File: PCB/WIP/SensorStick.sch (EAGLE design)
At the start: 84 parts, among them U1 TPD4F003DQDR, U10 LIS3MDLTR, U11 LIS3MDLTR, U2 BMI088, U3 BMI088, U4 BMI088, U5 STM32H743ZIT6, U9 LIS3MDLTR, Y1 ECS-TXO-3225MV-400-TR

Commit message: starting on board
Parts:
- removed AIRSPEED: 4525DO-DS5AI001DP, 4525DO-DS5AI001DP:4525DO-DS5AI001DP
- removed C3: 0.1uF, SparkFun-Capacitors:0.1UF-0402-6.3V-10%-X7R
- added R19, R20, R21, R22: RT0402FRE07220RL, ce-capstone:RT0402FRE07220RL
- R6, R7: value 4.7k -> RT0402FRE07220RL; device SparkFun-Resistors:4.7KOHM-0603-1/10W-1% -> ce-capstone:RT0402FRE07220RL
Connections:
- new net N$13: R6.2, U5G$3.PD7
- new net N$14: R7.2, U5G$3.PD6
- net 3V3: no longer R6.2, R7.1
- net 5V: no longer AIRSPEED.VCC, C3.2
- net CSB_ACCEL1: now also R19.2
- net CSB_ACCEL2: now also R21.2
- net CSB_ACCEL3: now also R6.1
- net CSB_GYRO1: now also R20.2
- net CSB_GYRO2: now also R7.1
- net CSB_GYRO3: now also U5G$3.PD10
- net EXTI3: no longer AIRSPEED.INT_(I2C)_/_SS_(SPI)
- net GND: now also Y1.GROUND; no longer AIRSPEED.GROUND, C3.1
- net I2C3_SCL: no longer AIRSPEED.SCL_(I2C)_/_SCLK_(SPI), R6.1
- net I2C3_SDA: no longer AIRSPEED.SDA_(I2C)_/_MISO_(SPI), R7.2
- net SPI1_MISO: no longer U4.SDO2
- net SPI2_MISO: no longer U3.SDO2
- net SPI3_MISO: no longer U2.SDO2
- net USART2_RX: now also U5G$1.PA3
- net USART2_TX: now also U5G$1.PA2
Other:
- moved on the sheet: R11, R6, R7, R8, R9, Y1

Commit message: snapshot
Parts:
- removed R22: RT0402FRE07220RL, ce-capstone:RT0402FRE07220RL
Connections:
- net SPI1_CS renamed JTDI
- new net JTRST: U5G$2.PB4(!JTRST!)
- new net TRACESWO: U5G$2.PB3(JTDO/TRACESWO)
- net NRST: now also U5G$1.!RST
- net SPI3_MISO: now also U5G$2.PC11; no longer U5G$2.PB4(!JTRST!)
- net SPI3_SCK: now also U5G$2.PC10; no longer U5G$2.PB3(JTDO/TRACESWO)
- net SWCLK: now also U5G$1.PA14(JTCK/SWCLK)
- net SWDIO: now also U5G$1.PA13(JTMS-SWDIO)
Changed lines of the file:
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@@
 <part name="R20" library="ce-capstone" deviceset="RT0402FRE07220RL" device=""/>
 <part name="R21" library="ce-capstone" deviceset="RT0402FRE07220RL" device=""/>
-<part name="R22" library="ce-capstone" deviceset="RT0402FRE07220RL" device=""/>
 </parts>
 <sheets>
@@
 <instance part="R20" gate="G$1" x="147.32" y="147.32" smashed="yes"/>
 <instance part="R21" gate="G$1" x="147.32" y="144.78" smashed="yes"/>
-<instance part="R22" gate="G$1" x="200.66" y="134.62" smashed="yes">
-<attribute name="NAME" x="196.85" y="136.1186" size="1.778" layer="95"/>
-<attribute name="VALUE" x="196.85" y="131.318" size="1.778" layer="96"/>
-</instance>
 </instances>
 <busses>
@@
 <label x="215.9" y="172.72" size="1.778" layer="95"/>
 </segment>
+<segment>
+<pinref part="U5" gate="G$1" pin="!RST"/>
+<wire x1="106.68" y1="226.06" x2="116.84" y2="226.06" width="0.1524" layer="91"/>
+<label x="111.76" y="226.06" size="1.778" layer="95"/>
+</segment>
 </net>
 <net name="DP" class="0">
@@
 </segment>
 </net>
-<net name="SPI1_CS" class="0">
-<segment>
-<pinref part="U5" gate="G$1" pin="PA15(JTDI)"/>
-<wire x1="66.04" y1="187.96" x2="58.42" y2="187.96" width="0.1524" layer="91"/>
-<label x="55.88" y="187.96" size="1.778" layer="95"/>
-</segment>
-</net>
 <net name="I2C2_SDA" class="0">
 <segment>
@@
 <net name="SPI4_CS" class="0">
 <segment>
-<wire x1="144.78" y1="157.48" x2="154.94" y2="157.48" width="0.1524" layer="91"/>
-<label x="147.32" y="157.48" size="1.778" layer="95"/>
-<pinref part="U5" gate="G$3" pin="PE4"/>
-</segment>
-<segment>
 <pinref part="U9" gate="G$1" pin="CS"/>
 <wire x1="251.46" y1="33.02" x2="243.84" y2="33.02" width="0.1524" layer="91"/>
 <label x="241.3" y="33.02" size="1.778" layer="95"/>
 </segment>
+<segment>
+<pinref part="U5" gate="G$3" pin="PE4"/>
+<wire x1="144.78" y1="157.48" x2="154.94" y2="157.48" width="0.1524" layer="91"/>
+<label x="147.32" y="157.48" size="1.778" layer="95"/>
+</segment>
 </net>
 <net name="SPI5_CS" class="0">
-<segment>
-<wire x1="160.02" y1="180.34" x2="152.4" y2="180.34" width="0.1524" layer="91"/>
-<label x="149.86" y="180.34" size="1.778" layer="95"/>
-<pinref part="U5" gate="G$4" pin="PF6"/>
-</segment>
 <segment>
 <pinref part="U11" gate="G$1" pin="CS"/>
@@
 <label x="187.96" y="284.48" size="1.778" layer="95"/>
 </segment>
+<segment>
+<pinref part="U5" gate="G$4" pin="PF6"/>
+<wire x1="160.02" y1="180.34" x2="152.4" y2="180.34" width="0.1524" layer="91"/>
+<label x="149.86" y="180.34" size="1.778" layer="95"/>
+</segment>
 </net>
 <net name="SPI5_SCK" class="0">
@@
 <net name="SPI6_CS" class="0">
 <segment>
-<wire x1="195.58" y1="175.26" x2="205.74" y2="175.26" width="0.1524" layer="91"/>
-<label x="198.12" y="175.26" size="1.778" layer="95"/>
-<pinref part="U5" gate="G$4" pin="PG8"/>
-</segment>
-<segment>
 <pinref part="U10" gate="G$1" pin="CS"/>
 <wire x1="15.24" y1="287.02" x2="7.62" y2="287.02" width="0.1524" layer="91"/>
 <label x="5.08" y="287.02" size="1.778" layer="95"/>
 </segment>
+<segment>
+<pinref part="U5" gate="G$4" pin="PG8"/>
+<wire x1="195.58" y1="175.26" x2="203.2" y2="175.26" width="0.1524" layer="91"/>
+<wire x1="205.74" y1="175.26" x2="203.2" y2="175.26" width="0.1524" layer="91"/>
+<label x="198.12" y="175.26" size="1.778" layer="95"/>
+</segment>
 </net>
 <net name="I2C4_SCL" class="0">
@@
 <net name="SPI3_MISO" class="0">
 <segment>
-<wire x1="139.7" y1="243.84" x2="132.08" y2="243.84" width="0.1524" layer="91"/>
-<label x="127" y="243.84" size="1.778" layer="95"/>
-<pinref part="U5" gate="G$2" pin="PB4(!JTRST!)"/>
-</segment>
-<segment>
 <pinref part="U2" gate="G$1" pin="SDO1"/>
 <wire x1="327.66" y1="76.2" x2="335.28" y2="76.2" width="0.1524" layer="91"/>
 <label x="325.12" y="76.2" size="1.778" layer="95"/>
 </segment>
+<segment>
+<pinref part="U5" gate="G$2" pin="PC11"/>
+<wire x1="185.42" y1="226.06" x2="193.04" y2="226.06" width="0.1524" layer="91"/>
+<label x="187.96" y="226.06" size="1.778" layer="95"/>
+</segment>
 </net>
 <net name="SPI3_MOSI" class="0">
@@
 <net name="SPI3_SCK" class="0">
 <segment>
-<wire x1="139.7" y1="246.38" x2="132.08" y2="246.38" width="0.1524" layer="91"/>
-<label x="127" y="246.38" size="1.778" layer="95"/>
-<pinref part="U5" gate="G$2" pin="PB3(JTDO/TRACESWO)"/>
-</segment>
-<segment>
 <pinref part="U2" gate="G$1" pin="SCL/SCK"/>
 <wire x1="292.1" y1="66.04" x2="284.48" y2="66.04" width="0.1524" layer="91"/>
 <label x="281.94" y="66.04" size="1.778" layer="95"/>
 </segment>
+<segment>
+<pinref part="U5" gate="G$2" pin="PC10"/>
+<wire x1="185.42" y1="228.6" x2="193.04" y2="228.6" width="0.1524" layer="91"/>
+<label x="187.96" y="228.6" size="1.778" layer="95"/>
+</segment>
 </net>
 <net name="SPI2_SCK" class="0">
@@
 <pinref part="U1" gate="A" pin="CH3_IN"/>
 </segment>
+<segment>
+<pinref part="U5" gate="G$1" pin="PA13(JTMS-SWDIO)"/>
+<wire x1="66.04" y1="193.04" x2="55.88" y2="193.04" width="0.1524" layer="91"/>
+<label x="55.88" y="193.04" size="1.778" layer="95"/>
+</segment>
 </net>
 <net name="SWCLK" class="0">
@@
 <wire x1="276.86" y1="139.7" x2="256.54" y2="139.7" width="0.1524" layer="91"/>
 <pinref part="U1" gate="A" pin="CH2_IN"/>
+</segment>
+<segment>
+<pinref part="U5" gate="G$1" pin="PA14(JTCK/SWCLK)"/>
+<wire x1="66.04" y1="190.5" x2="55.88" y2="190.5" width="0.1524" layer="91"/>
+<label x="55.88" y="190.5" size="1.778" layer="95"/>
 </segment>
 </net>
@@
 </segment>
 </net>
+<net name="JTDI" class="0">
+<segment>
+<pinref part="U5" gate="G$1" pin="PA15(JTDI)"/>
+<wire x1="66.04" y1="187.96" x2="55.88" y2="187.96" width="0.1524" layer="91"/>
+<label x="55.88" y="187.96" size="1.778" layer="95"/>
+</segment>
+</net>
+<net name="TRACESWO" class="0">
+<segment>
+<pinref part="U5" gate="G$2" pin="PB3(JTDO/TRACESWO)"/>
+<wire x1="139.7" y1="246.38" x2="132.08" y2="246.38" width="0.1524" layer="91"/>
+<label x="129.54" y="246.38" size="1.778" layer="95"/>
+</segment>
+</net>
+<net name="JTRST" class="0">
+<segment>
+<pinref part="U5" gate="G$2" pin="PB4(!JTRST!)"/>
+<wire x1="139.7" y1="243.84" x2="132.08" y2="243.84" width="0.1524" layer="91"/>
+<label x="129.54" y="243.84" size="1.778" layer="95"/>
+</segment>
+</net>

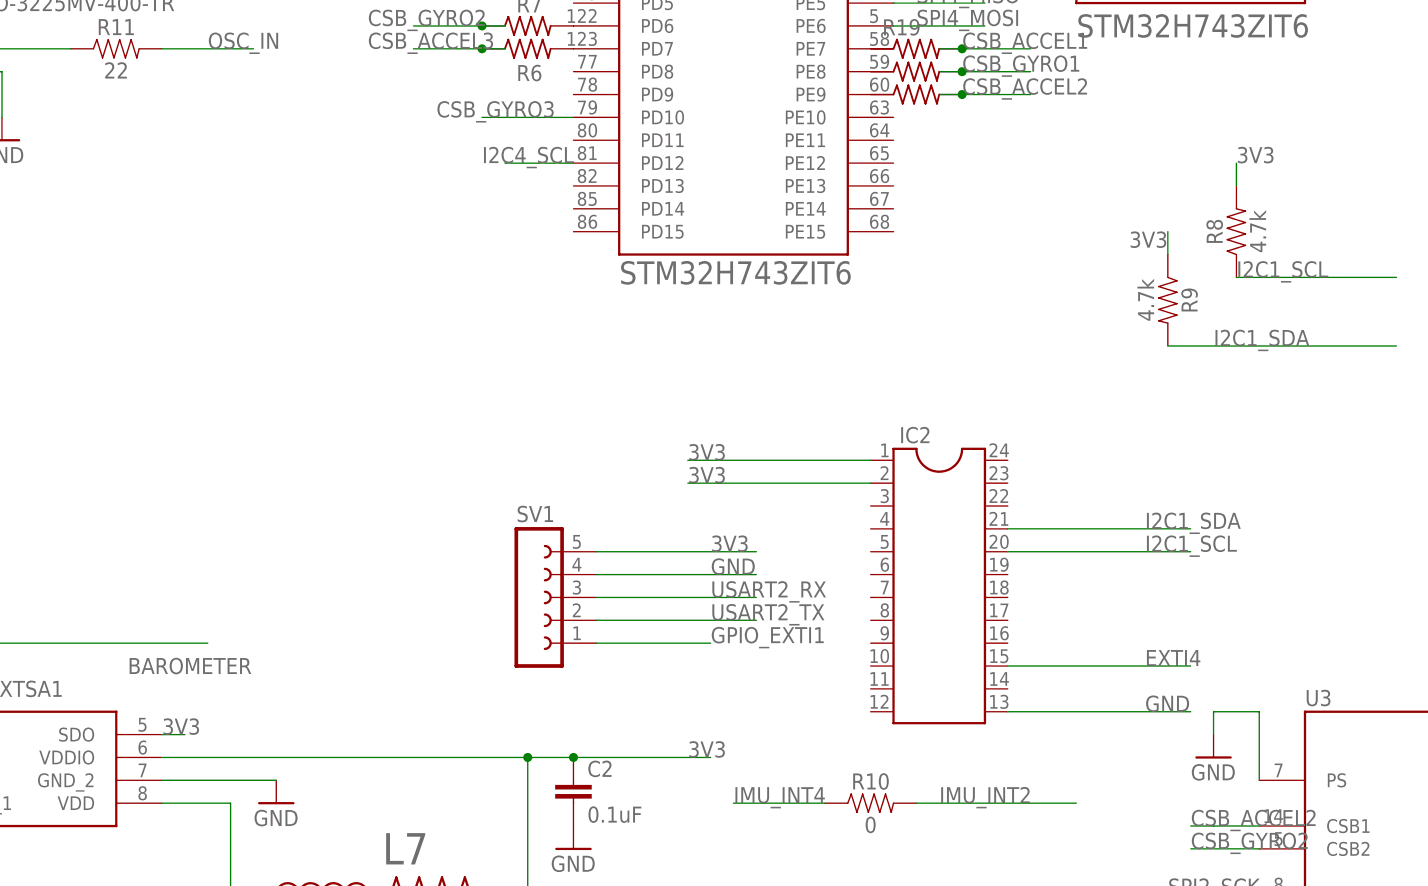
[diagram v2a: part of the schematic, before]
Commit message: added in JST connections, still need to resolve extra SPI connection
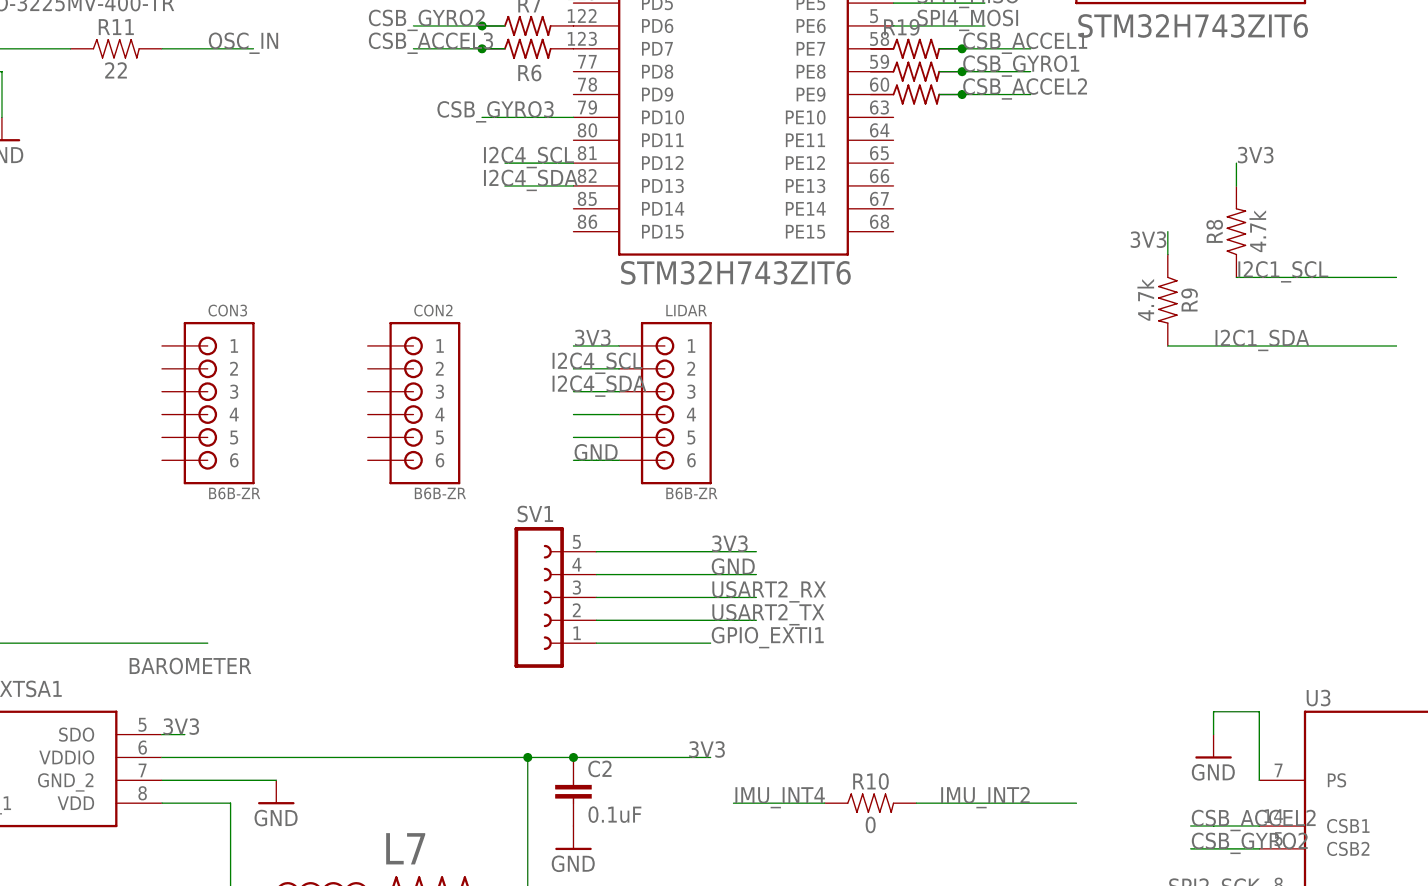
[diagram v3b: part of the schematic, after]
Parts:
- removed IC2: (no value), ic-package:DIL24-6
- added CON2, CON3, LIDAR: B6B-ZR, jst:B6B-ZR
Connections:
- new net N$21: LIDAR.5
- new net N$22: LIDAR.4
- net 3V3: now also LIDAR.1; no longer IC2.1, IC2.2
- net EXTI4: no longer IC2.15
- net GND: now also LIDAR.6; no longer IC2.13
- net I2C1_SCL: no longer IC2.20
- net I2C1_SDA: no longer IC2.21
- net I2C4_SCL: now also LIDAR.2
- net I2C4_SDA: now also LIDAR.3, U5G$3.PD13
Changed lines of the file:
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@@
 <part name="C27" library="capacitor-wima" library_urn="urn:adsk.eagle:library:116" deviceset="C" device="2.5/4" package3d_urn="urn:adsk.eagle:package:5408/1"/>
 <part name="JP7" library="pinhead" library_urn="urn:adsk.eagle:library:325" deviceset="PINHD-2X3" device="" package3d_urn="urn:adsk.eagle:package:22462/2"/>
-<part name="IC2" library="ic-package" library_urn="urn:adsk.eagle:library:239" deviceset="DIL24" device="-6" package3d_urn="urn:adsk.eagle:package:1009/2"/>
 <part name="U2" library="BMI088" deviceset="BMI088" device=""/>
 <part name="GND33" library="supply1" library_urn="urn:adsk.eagle:library:371" deviceset="GND" device=""/>
@@
 <part name="R20" library="ce-capstone" deviceset="RT0402FRE07220RL" device=""/>
 <part name="R21" library="ce-capstone" deviceset="RT0402FRE07220RL" device=""/>
+<part name="LIDAR" library="jst" deviceset="B6B-ZR" device=""/>
+<part name="CON2" library="jst" deviceset="B6B-ZR" device=""/>
+<part name="CON3" library="jst" deviceset="B6B-ZR" device=""/>
 </parts>
 <sheets>
@@
 <attribute name="VALUE" x="344.17" y="104.14" size="1.778" layer="96"/>
 </instance>
-<instance part="IC2" gate="G$1" x="149.86" y="88.9" smashed="yes">
-<attribute name="NAME" x="145.415" y="106.045" size="1.778" layer="95"/>
-<attribute name="VALUE" x="145.415" y="72.39" size="1.778" layer="96"/>
-</instance>
 <instance part="U2" gate="G$1" x="309.88" y="68.58" smashed="yes">
 <attribute name="NAME" x="297.18" y="86.995" size="1.778" layer="95"/>
@@
 <instance part="R20" gate="G$1" x="147.32" y="147.32" smashed="yes"/>
 <instance part="R21" gate="G$1" x="147.32" y="144.78" smashed="yes"/>
+<instance part="LIDAR" gate="G$1" x="119.38" y="116.84" smashed="yes">
+<attribute name="NAME" x="119.38" y="120.142" size="1.27" layer="95"/>
+<attribute name="VALUE" x="119.38" y="99.822" size="1.27" layer="96"/>
+</instance>
+<instance part="CON2" gate="G$1" x="91.44" y="116.84" smashed="yes">
+<attribute name="NAME" x="91.44" y="120.142" size="1.27" layer="95"/>
+<attribute name="VALUE" x="91.44" y="99.822" size="1.27" layer="96"/>
+</instance>
+<instance part="CON3" gate="G$1" x="68.58" y="116.84" smashed="yes">
+<attribute name="NAME" x="68.58" y="120.142" size="1.27" layer="95"/>
+<attribute name="VALUE" x="68.58" y="99.822" size="1.27" layer="96"/>
+</instance>
 </instances>
 <busses>
@@
 </segment>
 <segment>
-<wire x1="142.24" y1="104.14" x2="121.92" y2="104.14" width="0.1524" layer="91"/>
-<pinref part="IC2" gate="G$1" pin="1"/>
-<label x="121.92" y="104.14" size="1.778" layer="95"/>
-</segment>
-<segment>
-<wire x1="142.24" y1="101.6" x2="121.92" y2="101.6" width="0.1524" layer="91"/>
-<pinref part="IC2" gate="G$1" pin="2"/>
-<label x="121.92" y="101.6" size="1.778" layer="95"/>
-</segment>
-<segment>
 <pinref part="U9" gate="G$1" pin="VDD_IO"/>
 <wire x1="281.94" y1="40.64" x2="287.02" y2="40.64" width="0.1524" layer="91"/>
@@
 <wire x1="182.88" y1="134.62" x2="182.88" y2="137.16" width="0.1524" layer="91"/>
 <label x="182.88" y="137.16" size="1.778" layer="95"/>
+</segment>
+<segment>
+<wire x1="114.3" y1="116.84" x2="109.22" y2="116.84" width="0.1524" layer="91"/>
+<label x="109.22" y="116.84" size="1.778" layer="95"/>
+<pinref part="LIDAR" gate="G$1" pin="1"/>
 </segment>
 </net>
@@
 </segment>
 <segment>
-<wire x1="157.48" y1="76.2" x2="177.8" y2="76.2" width="0.1524" layer="91"/>
-<label x="172.72" y="76.2" size="1.778" layer="95"/>
-<pinref part="IC2" gate="G$1" pin="13"/>
-</segment>
-<segment>
 <pinref part="U2" gate="G$1" pin="GNDA"/>
 <wire x1="327.66" y1="53.34" x2="337.82" y2="53.34" width="0.1524" layer="91"/>
@@
 <wire x1="40.64" y1="147.32" x2="45.72" y2="147.32" width="0.1524" layer="91"/>
 </segment>
+<segment>
+<pinref part="LIDAR" gate="G$1" pin="6"/>
+<wire x1="114.3" y1="104.14" x2="111.76" y2="104.14" width="0.1524" layer="91"/>
+<wire x1="109.22" y1="104.14" x2="111.76" y2="104.14" width="0.1524" layer="91"/>
+<label x="109.22" y="104.14" size="1.778" layer="95"/>
+</segment>
 </net>
 <net name="I2C2_SCL" class="0">
@@
 </segment>
 <segment>
-<label x="172.72" y="96.52" size="1.778" layer="95"/>
-<pinref part="IC2" gate="G$1" pin="21"/>
-<wire x1="177.8" y1="96.52" x2="157.48" y2="96.52" width="0.1524" layer="91"/>
-</segment>
-<segment>
 <pinref part="BAROMETER" gate="G$1" pin="SDI"/>
 <wire x1="33.02" y1="71.12" x2="10.16" y2="71.12" width="0.1524" layer="91"/>
@@
 <label x="127" y="233.68" size="1.778" layer="95"/>
 <pinref part="U5" gate="G$2" pin="PB8"/>
-</segment>
-<segment>
-<label x="172.72" y="93.98" size="1.778" layer="95"/>
-<pinref part="IC2" gate="G$1" pin="20"/>
-<wire x1="177.8" y1="93.98" x2="157.48" y2="93.98" width="0.1524" layer="91"/>
 </segment>
 <segment>
@@
 <label x="35.56" y="203.2" size="1.778" layer="95"/>
 </segment>
-<segment>
-<wire x1="157.48" y1="81.28" x2="177.8" y2="81.28" width="0.1524" layer="91"/>
-<label x="172.72" y="81.28" size="1.778" layer="95"/>
-<pinref part="IC2" gate="G$1" pin="15"/>
-</segment>
 </net>
 <net name="USART2_TX" class="0">
@@
 <pinref part="U5" gate="G$3" pin="PD12"/>
 </segment>
+<segment>
+<wire x1="114.3" y1="114.3" x2="109.22" y2="114.3" width="0.1524" layer="91"/>
+<pinref part="LIDAR" gate="G$1" pin="2"/>
+<label x="106.68" y="114.3" size="1.778" layer="95"/>
+</segment>
 </net>
 <net name="LPUART1_TX" class="0">
@@
 <label x="127" y="236.22" size="1.778" layer="95"/>
 <pinref part="U5" gate="G$2" pin="PB7"/>
+</segment>
+<segment>
+<pinref part="U5" gate="G$3" pin="PD13"/>
+<wire x1="101.6" y1="134.62" x2="109.22" y2="134.62" width="0.1524" layer="91"/>
+<label x="99.06" y="134.62" size="1.778" layer="95"/>
+</segment>
+<segment>
+<wire x1="114.3" y1="111.76" x2="109.22" y2="111.76" width="0.1524" layer="91"/>
+<pinref part="LIDAR" gate="G$1" pin="3"/>
+<label x="106.68" y="111.76" size="1.778" layer="95"/>
 </segment>
 </net>
@@
 </segment>
 </net>
+<net name="N$21" class="0">
+<segment>
+<pinref part="LIDAR" gate="G$1" pin="5"/>
+<wire x1="114.3" y1="106.68" x2="109.22" y2="106.68" width="0.1524" layer="91"/>
+</segment>
+</net>
+<net name="N$22" class="0">
+<segment>
+<pinref part="LIDAR" gate="G$1" pin="4"/>
+<wire x1="114.3" y1="109.22" x2="109.22" y2="109.22" width="0.1524" layer="91"/>
+</segment>
+</net>
